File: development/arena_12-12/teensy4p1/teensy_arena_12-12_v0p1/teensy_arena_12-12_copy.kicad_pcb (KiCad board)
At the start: 4 copper layers, 228.6 x 228.6 mm, 51 parts, among them J1 Barrel_Jack, J2 Conn_01x04, J3 Conn_01x04, P1 CONN15, P10 CONN15, P11 CONN15, P12 CONN15, P2 CONN15, P3 CONN15, P4 CONN15, P5 CONN15, P6 CONN15, P7 CONN15, P8 CONN15, P9 CONN15, Q2 MOSFET_NCHAN, SW1 SW_SPDT, U1 TXB0108PW, U18 Teensy4.1, U2 TXB0108PW, U3 TXB0108PW, U4 TXB0108PW, U5 TXB0108PW

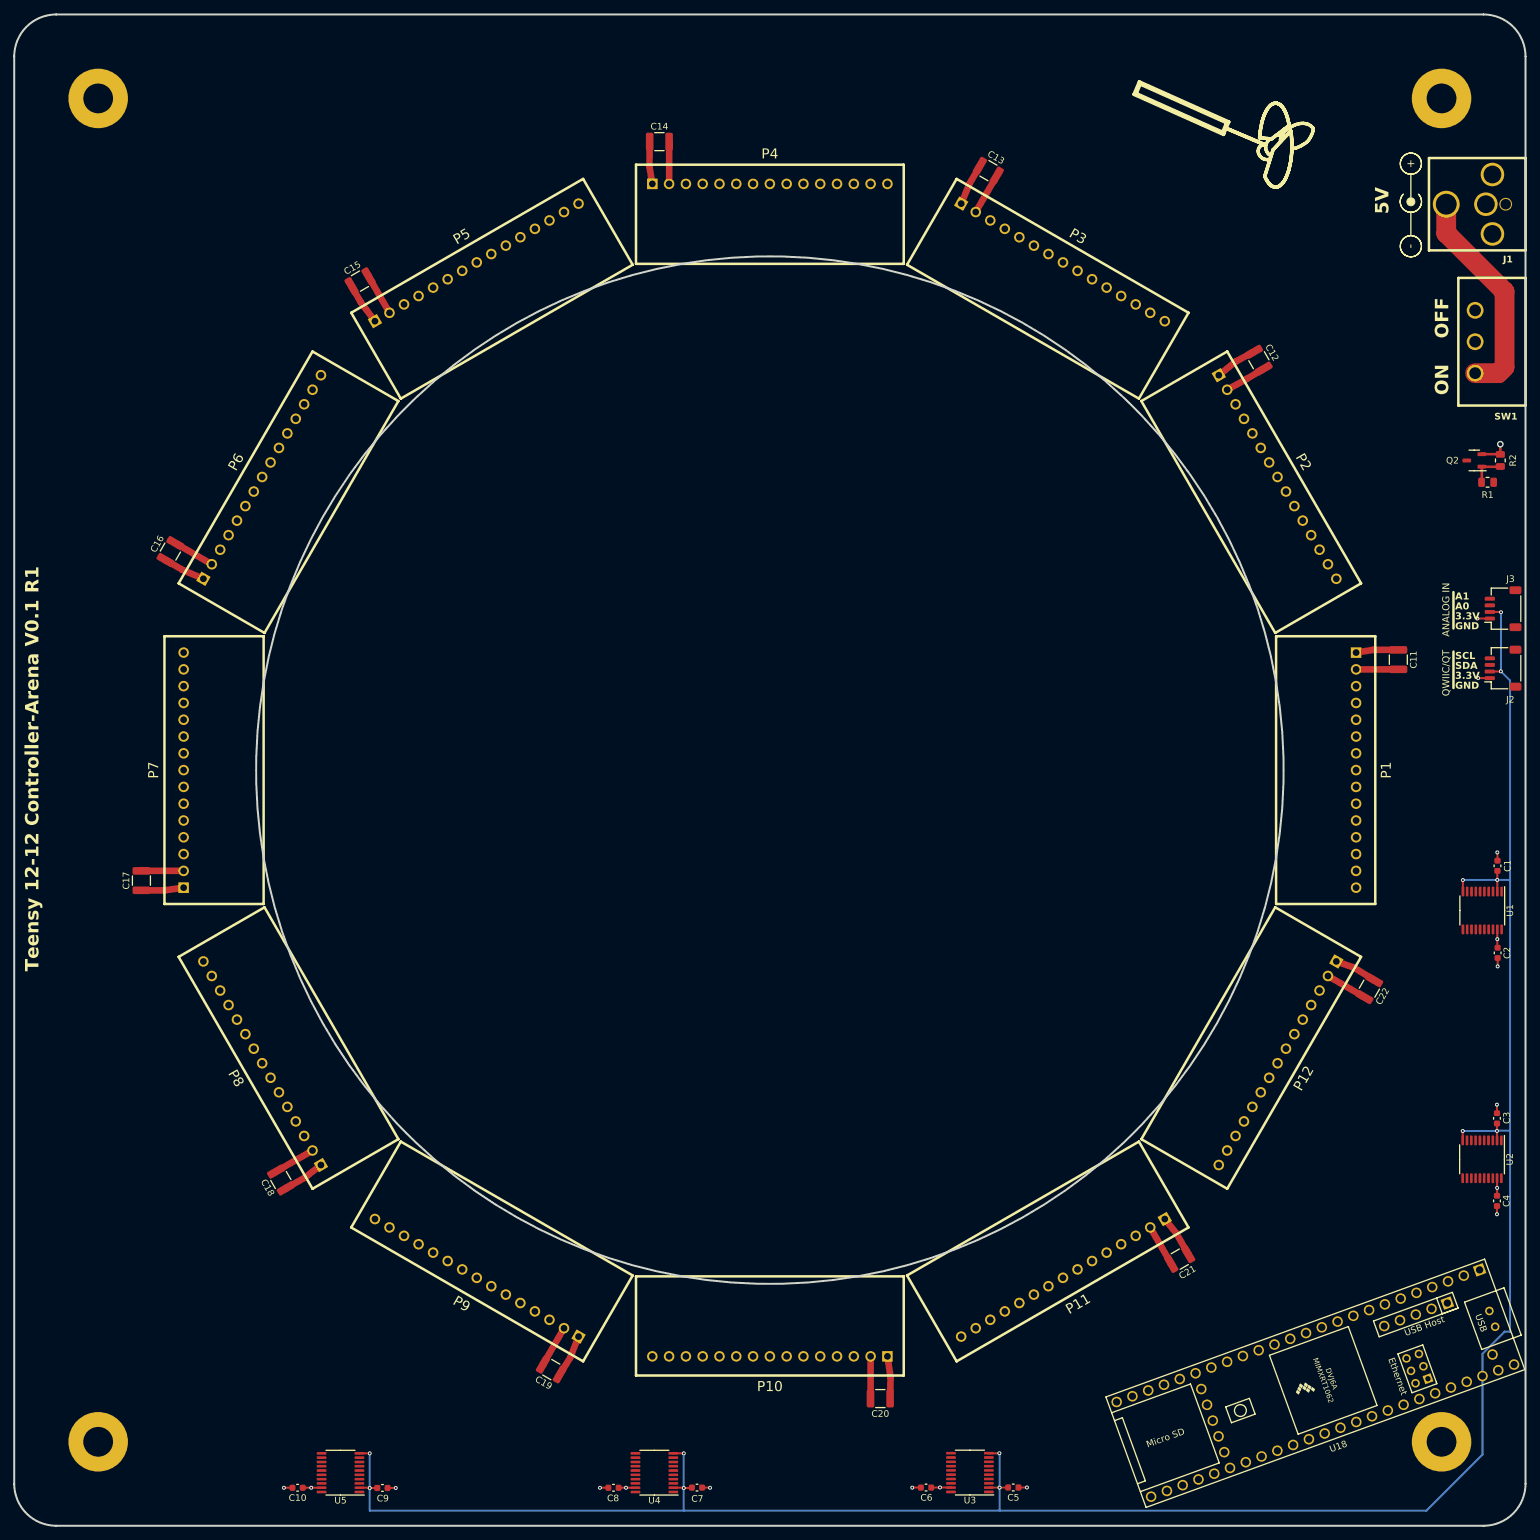
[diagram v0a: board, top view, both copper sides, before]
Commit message: Finished hand route of 12-12 teensy arena. Finished route of 12-12 top.
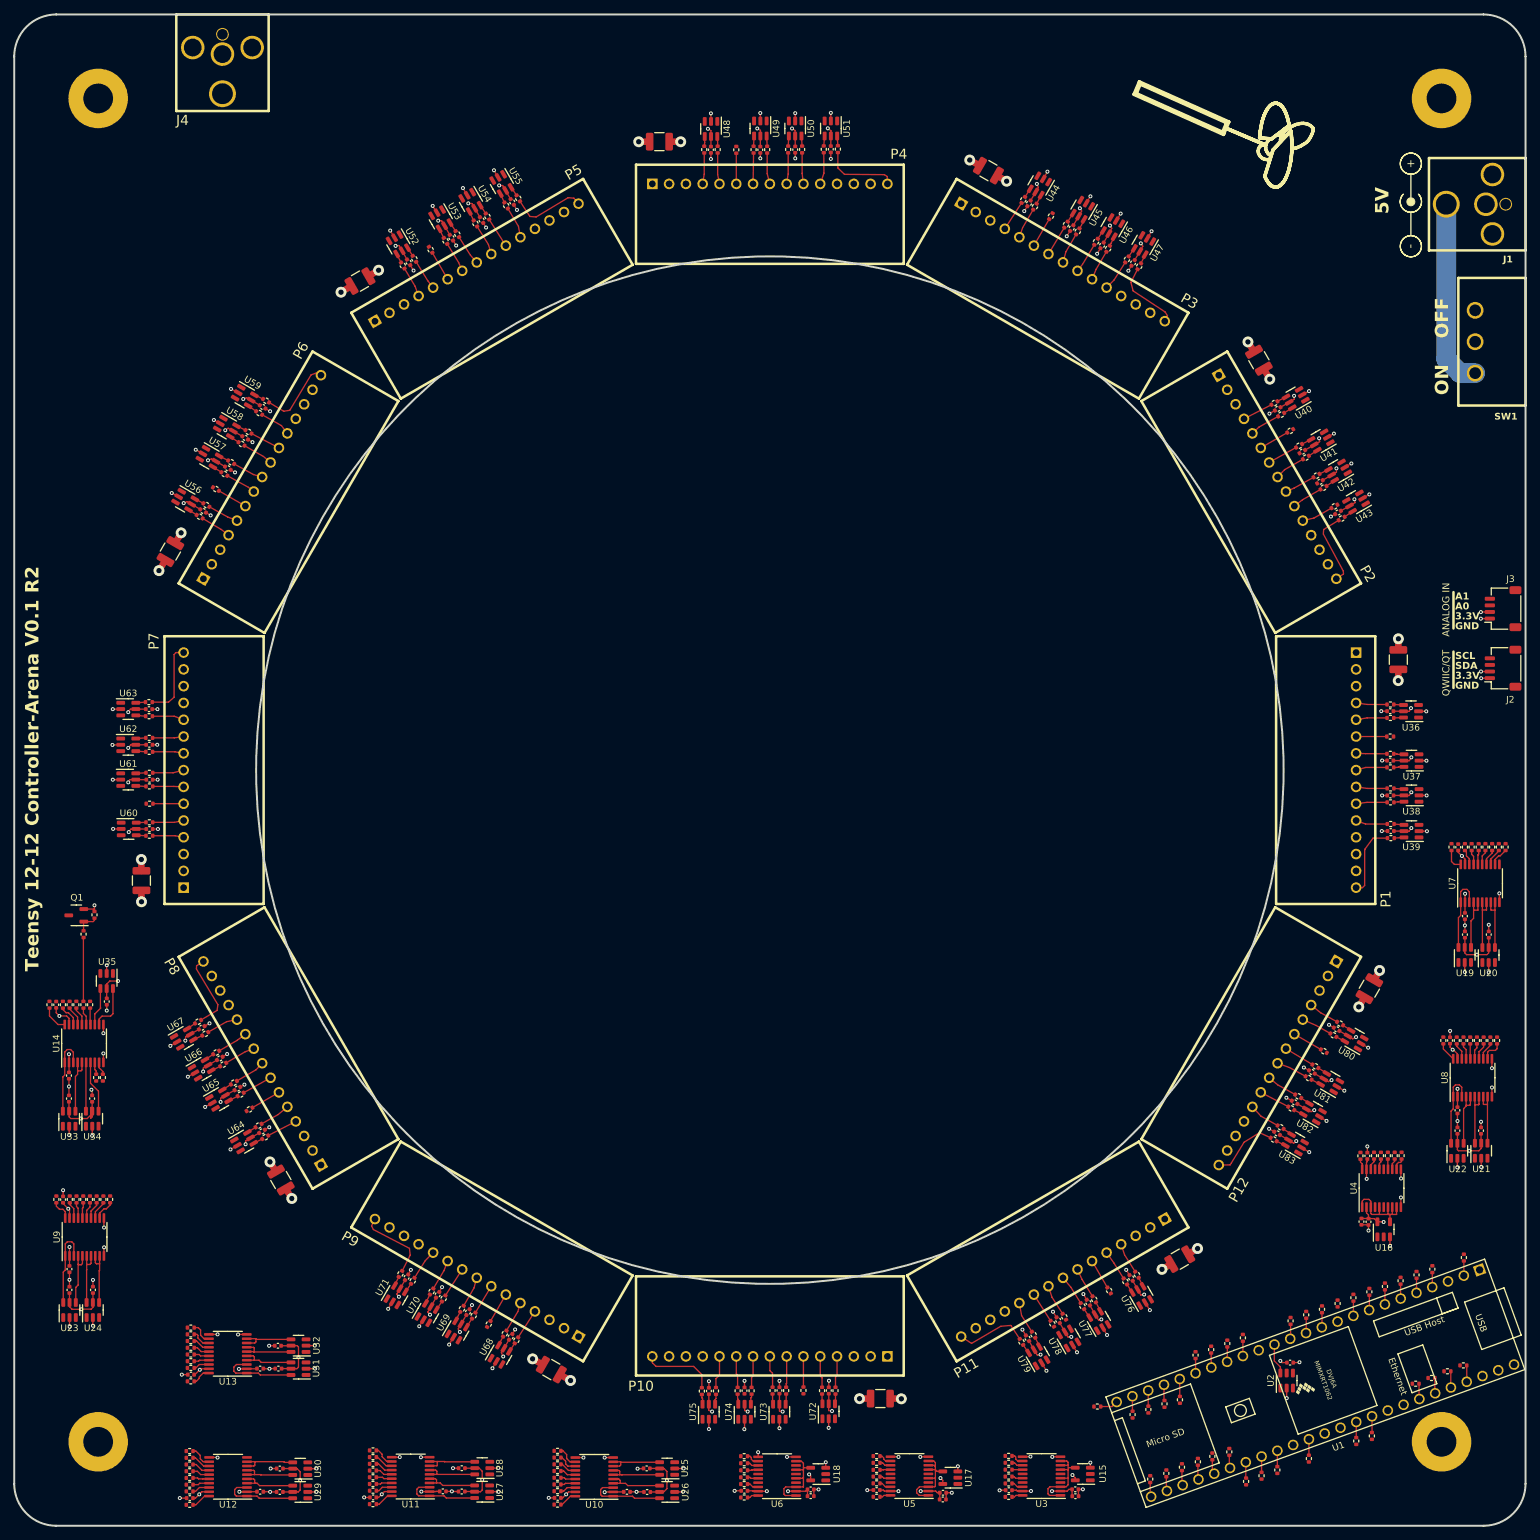
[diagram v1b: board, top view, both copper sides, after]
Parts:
- removed Q2: MOSFET_NCHAN, Package_TO_SOT_SMD:SOT-23-3
- removed the U1 at (285.6, 199.0)
- added C11: 0.1uF, Capacitor_SMD:C_0402_1005Metric, F.Cu at (281.9, 189.5)
- added C12: 0.1uF, Capacitor_SMD:C_0402_1005Metric, F.Cu at (281.8, 229.3)
- added C13: 0.1uF, Capacitor_SMD:C_0402_1005Metric, F.Cu at (280.7, 218.7)
- added C14: 0.1uF, Capacitor_SMD:C_0402_1005Metric, F.Cu at (71.9, 253.3)
- added C15: 0.1uF, Capacitor_SMD:C_0402_1005Metric, F.Cu at (70.9, 242.8)
- added C16: 0.1uF, Capacitor_SMD:C_0402_1005Metric, F.Cu at (156.2, 287.0)
- added C17: 0.1uF, Capacitor_SMD:C_0402_1005Metric, F.Cu at (145.7, 287.9)
- added C18: 0.1uF, Capacitor_SMD:C_0402_1005Metric, F.Cu at (128.3, 286.9)
- added C19: 0.1uF, Capacitor_SMD:C_0402_1005Metric, F.Cu at (117.8, 287.8)
- added C20: 0.1uF, Capacitor_SMD:C_0402_1005Metric, F.Cu at (100.7, 287.0)
- added C21: 0.1uF, Capacitor_SMD:C_0402_1005Metric, F.Cu at (90.1, 287.9)
- added C22: 0.1uF, Capacitor_SMD:C_0402_1005Metric, F.Cu at (100.7, 268.3)
- added C23: 0.1uF, Capacitor_SMD:C_0402_1005Metric, F.Cu at (90.2, 269.2)
- added C24: 0.1uF, Capacitor_SMD:C_0402_1005Metric, F.Cu at (71.8, 224.0)
- added C25: 0.1uF, Capacitor_SMD:C_0402_1005Metric, F.Cu at (69.8, 213.3)
- added C26: 0.1uF, Capacitor_SMD:C_0402_1005Metric, F.Cu at (224.0, 286.6)
- added C27: 0.1uF, Capacitor_SMD:C_0402_1005Metric, F.Cu at (268.4, 246.1)
- added C28: 0.1uF, Capacitor_SMD:C_0402_1005Metric, F.Cu at (204.0, 287.1)
- added C29: 0.1uF, Capacitor_SMD:C_0402_1005Metric, F.Cu at (184.0, 286.6)
- added C30: 0.1uF, Capacitor_SMD:C_0402_1005Metric, F.Cu at (282.9, 202.7)
- added C31: 0.1uF, Capacitor_SMD:C_0402_1005Metric, F.Cu at (286.5, 202.7)
- added C32: 0.1uF, Capacitor_SMD:C_0402_1005Metric, F.Cu at (281.8, 232.3)
- added C33: 0.1uF, Capacitor_SMD:C_0402_1005Metric, F.Cu at (285.4, 232.3)
- added C34: 0.1uF, Capacitor_SMD:C_0402_1005Metric, F.Cu at (71.9, 256.4)
- added C35: 0.1uF, Capacitor_SMD:C_0402_1005Metric, F.Cu at (75.4, 256.4)
- added C36: 0.1uF, Capacitor_SMD:C_0402_1005Metric, F.Cu at (159.2, 283.4)
- added C37: 0.1uF, Capacitor_SMD:C_0402_1005Metric, F.Cu at (159.2, 287.0)
- added C38: 0.1uF, Capacitor_SMD:C_0402_1005Metric, F.Cu at (131.2, 286.9)
- added C39: 0.1uF, Capacitor_SMD:C_0402_1005Metric, F.Cu at (131.2, 283.4)
- added C40: 0.1uF, Capacitor_SMD:C_0402_1005Metric, F.Cu at (103.7, 287.0)
- added C41: 0.1uF, Capacitor_SMD:C_0402_1005Metric, F.Cu at (103.7, 283.4)
- added C42: 0.1uF, Capacitor_SMD:C_0402_1005Metric, F.Cu at (103.5, 268.3)
- added C43: 0.1uF, Capacitor_SMD:C_0402_1005Metric, F.Cu at (103.4, 264.9)
- added C44: 0.1uF, Capacitor_SMD:C_0402_1005Metric, F.Cu at (71.8, 227.5)
- added C45: 0.1uF, Capacitor_SMD:C_0402_1005Metric, F.Cu at (75.3, 227.5)
- added C46: 0.1uF, Capacitor_SMD:C_0402_1005Metric, F.Cu at (77.5, 212.8)
- added C47: 0.1uF, Capacitor_SMD:C_0402_1005Metric, F.Cu at (271.6, 168.9)
- added C48: 0.1uF, Capacitor_SMD:C_0402_1005Metric, F.Cu at (271.6, 176.4)
- added C49: 0.1uF, Capacitor_SMD:C_0402_1005Metric, F.Cu at (271.7, 181.6)
- added C50: 0.1uF, Capacitor_SMD:C_0402_1005Metric, F.Cu at (271.7, 187.0)
- added C51: 0.1uF, Capacitor_SMD:C_0402_1005Metric, F.Cu at (254.6, 123.2)
- added C52: 0.1uF, Capacitor_SMD:C_0402_1005Metric, F.Cu at (258.3, 129.6)
- added C53: 0.1uF, Capacitor_SMD:C_0402_1005Metric, F.Cu at (261.0, 134.2)
- added C54: 0.1uF, Capacitor_SMD:C_0402_1005Metric, F.Cu at (263.7, 138.8)
- added C55: 0.1uF, Capacitor_SMD:C_0402_1005Metric, F.Cu at (217.0, 92.1)
- added C56: 0.1uF, Capacitor_SMD:C_0402_1005Metric, F.Cu at (223.5, 95.8)
- added C57: 0.1uF, Capacitor_SMD:C_0402_1005Metric, F.Cu at (228.1, 98.4)
- added C58: 0.1uF, Capacitor_SMD:C_0402_1005Metric, F.Cu at (232.7, 101.1)
- added C59: 0.1uF, Capacitor_SMD:C_0402_1005Metric, F.Cu at (168.9, 84.0)
- added C60: 0.1uF, Capacitor_SMD:C_0402_1005Metric, F.Cu at (176.4, 84.0)
- added C61: 0.1uF, Capacitor_SMD:C_0402_1005Metric, F.Cu at (181.6, 83.9)
- added C62: 0.1uF, Capacitor_SMD:C_0402_1005Metric, F.Cu at (187.0, 83.9)
- added C63: 0.1uF, Capacitor_SMD:C_0402_1005Metric, F.Cu at (123.2, 101.0)
- added C64: 0.1uF, Capacitor_SMD:C_0402_1005Metric, F.Cu at (129.6, 97.3)
- added C65: 0.1uF, Capacitor_SMD:C_0402_1005Metric, F.Cu at (134.2, 94.6)
- added C66: 0.1uF, Capacitor_SMD:C_0402_1005Metric, F.Cu at (138.8, 91.9)
- added C67: 0.1uF, Capacitor_SMD:C_0402_1005Metric, F.Cu at (92.1, 138.6)
- added C68: 0.1uF, Capacitor_SMD:C_0402_1005Metric, F.Cu at (95.8, 132.1)
- added C69: 0.1uF, Capacitor_SMD:C_0402_1005Metric, F.Cu at (98.4, 127.5)
- added C70: 0.1uF, Capacitor_SMD:C_0402_1005Metric, F.Cu at (101.1, 122.9)
- added C71: 0.1uF, Capacitor_SMD:C_0402_1005Metric, F.Cu at (84.0, 186.7)
- added C72: 0.1uF, Capacitor_SMD:C_0402_1005Metric, F.Cu at (84.0, 179.2)
- added C73: 0.1uF, Capacitor_SMD:C_0402_1005Metric, F.Cu at (83.9, 174.0)
- added C74: 0.1uF, Capacitor_SMD:C_0402_1005Metric, F.Cu at (83.9, 168.6)
- added C75: 0.1uF, Capacitor_SMD:C_0402_1005Metric, F.Cu at (101.0, 232.4)
- added C76: 0.1uF, Capacitor_SMD:C_0402_1005Metric, F.Cu at (97.3, 226.0)
- added C77: 0.1uF, Capacitor_SMD:C_0402_1005Metric, F.Cu at (94.6, 221.4)
- added C78: 0.1uF, Capacitor_SMD:C_0402_1005Metric, F.Cu at (91.9, 216.8)
- added C79: 0.1uF, Capacitor_SMD:C_0402_1005Metric, F.Cu at (138.6, 263.5)
- added C80: 0.1uF, Capacitor_SMD:C_0402_1005Metric, F.Cu at (132.1, 259.8)
- added C81: 0.1uF, Capacitor_SMD:C_0402_1005Metric, F.Cu at (127.5, 257.2)
- added C82: 0.1uF, Capacitor_SMD:C_0402_1005Metric, F.Cu at (122.9, 254.5)
- added C83: 0.1uF, Capacitor_SMD:C_0402_1005Metric, F.Cu at (186.7, 271.6)
- added C84: 0.1uF, Capacitor_SMD:C_0402_1005Metric, F.Cu at (179.2, 271.6)
- added C85: 0.1uF, Capacitor_SMD:C_0402_1005Metric, F.Cu at (174.0, 271.7)
- added C86: 0.1uF, Capacitor_SMD:C_0402_1005Metric, F.Cu at (168.6, 271.7)
- added C87: 0.1uF, Capacitor_SMD:C_0402_1005Metric, F.Cu at (232.4, 254.6)
- added C88: 0.1uF, Capacitor_SMD:C_0402_1005Metric, F.Cu at (226.0, 258.3)
- added C89: 0.1uF, Capacitor_SMD:C_0402_1005Metric, F.Cu at (221.4, 261.0)
- added C90: 0.1uF, Capacitor_SMD:C_0402_1005Metric, F.Cu at (216.8, 263.7)
- added C91: 0.1uF, Capacitor_SMD:C_0402_1005Metric, F.Cu at (263.5, 217.0)
- added C92: 0.1uF, Capacitor_SMD:C_0402_1005Metric, F.Cu at (259.8, 223.5)
- added C93: 0.1uF, Capacitor_SMD:C_0402_1005Metric, F.Cu at (257.2, 228.1)
- added C94: 0.1uF, Capacitor_SMD:C_0402_1005Metric, F.Cu at (254.5, 232.7)
- added J4: Barrel_Jack, arena_custom:DCJACK_2PIN_HIGHCURRENT, F.Cu at (95.0, 63.5)
- added Q1: MOSFET_NCHAN, Package_TO_SOT_SMD:SOT-23-3, F.Cu at (72.9, 199.8)
- added R10: 68, Resistor_SMD:R_0402_1005Metric, F.Cu at (275.6, 254.2)
- added R100: 68, Resistor_SMD:R_0402_1005Metric, F.Cu at (117.8, 282.7)
- added R101: 68, Resistor_SMD:R_0402_1005Metric, F.Cu at (117.8, 281.7)
- added R102: 68, Resistor_SMD:R_0402_1005Metric, F.Cu at (117.8, 280.7)
- added R103: 68, Resistor_SMD:R_0402_1005Metric, F.Cu at (90.0, 288.9)
- added R104: 68, Resistor_SMD:R_0402_1005Metric, F.Cu at (90.0, 286.9)
- added R105: 68, Resistor_SMD:R_0402_1005Metric, F.Cu at (90.0, 285.9)
- added R106: 68, Resistor_SMD:R_0402_1005Metric, F.Cu at (90.0, 284.9)
- added R107: 68, Resistor_SMD:R_0402_1005Metric, F.Cu at (90.0, 283.9)
- added R108: 68, Resistor_SMD:R_0402_1005Metric, F.Cu at (90.0, 282.8)
- added R109: 68, Resistor_SMD:R_0402_1005Metric, F.Cu at (90.0, 281.8)
- added R11: 68, Resistor_SMD:R_0402_1005Metric, F.Cu at (273.2, 255.0)
- added R110: 68, Resistor_SMD:R_0402_1005Metric, F.Cu at (90.0, 280.8)
- added R111: 68, Resistor_SMD:R_0402_1005Metric, F.Cu at (90.2, 270.3)
- added R112: 68, Resistor_SMD:R_0402_1005Metric, F.Cu at (90.2, 268.2)
- added R113: 68, Resistor_SMD:R_0402_1005Metric, F.Cu at (90.2, 267.2)
- added R114: 68, Resistor_SMD:R_0402_1005Metric, F.Cu at (90.2, 266.2)
- added R115: 68, Resistor_SMD:R_0402_1005Metric, F.Cu at (90.2, 265.2)
- added R116: 68, Resistor_SMD:R_0402_1005Metric, F.Cu at (90.2, 264.2)
- added R117: 68, Resistor_SMD:R_0402_1005Metric, F.Cu at (90.2, 263.1)
- added R118: 68, Resistor_SMD:R_0402_1005Metric, F.Cu at (90.2, 262.1)
- added R119: 68, Resistor_SMD:R_0402_1005Metric, F.Cu at (68.8, 213.3)
- added R12: 68, Resistor_SMD:R_0402_1005Metric, F.Cu at (270.8, 255.9)
- added R120: 68, Resistor_SMD:R_0402_1005Metric, F.Cu at (70.9, 213.3)
- added R121: 68, Resistor_SMD:R_0402_1005Metric, F.Cu at (71.9, 213.3)
- added R122: 68, Resistor_SMD:R_0402_1005Metric, F.Cu at (72.9, 213.3)
- added R123: 68, Resistor_SMD:R_0402_1005Metric, F.Cu at (74.0, 213.3)
- added R124: 68, Resistor_SMD:R_0402_1005Metric, F.Cu at (75.0, 213.3)
- added R125: 68, Resistor_SMD:R_0402_1005Metric, F.Cu at (75.9, 224.3)
- added R126: 68, Resistor_SMD:R_0402_1005Metric, F.Cu at (76.9, 224.3)
- added R127: 68, Resistor_SMD:R_0402_1005Metric, F.Cu at (271.7, 167.9)
- added R128: 68, Resistor_SMD:R_0402_1005Metric, F.Cu at (271.7, 169.9)
- added R129: 68, Resistor_SMD:R_0402_1005Metric, F.Cu at (271.7, 175.3)
- added R13: 68, Resistor_SMD:R_0402_1005Metric, F.Cu at (268.5, 256.7)
- added R130: 68, Resistor_SMD:R_0402_1005Metric, F.Cu at (271.7, 177.4)
- added R131: 68, Resistor_SMD:R_0402_1005Metric, F.Cu at (271.7, 180.6)
- added R132: 68, Resistor_SMD:R_0402_1005Metric, F.Cu at (271.7, 182.7)
- added R133: 68, Resistor_SMD:R_0402_1005Metric, F.Cu at (271.7, 186.0)
- added R134: 68, Resistor_SMD:R_0402_1005Metric, F.Cu at (271.7, 188.1)
- added R135: 68, Resistor_SMD:R_0402_1005Metric, F.Cu at (254.1, 122.3)
- added R136: 68, Resistor_SMD:R_0402_1005Metric, F.Cu at (255.1, 124.0)
- added R137: 68, Resistor_SMD:R_0402_1005Metric, F.Cu at (257.8, 128.7)
- added R138: 68, Resistor_SMD:R_0402_1005Metric, F.Cu at (258.9, 130.5)
- added R139: 68, Resistor_SMD:R_0402_1005Metric, F.Cu at (260.5, 133.3)
- added R14: 68, Resistor_SMD:R_0402_1005Metric, F.Cu at (266.1, 257.6)
- added R140: 68, Resistor_SMD:R_0402_1005Metric, F.Cu at (261.5, 135.1)
- added R141: 68, Resistor_SMD:R_0402_1005Metric, F.Cu at (263.2, 137.9)
- added R142: 68, Resistor_SMD:R_0402_1005Metric, F.Cu at (264.3, 139.7)
- added R143: 68, Resistor_SMD:R_0402_1005Metric, F.Cu at (216.1, 91.5)
- added R144: 68, Resistor_SMD:R_0402_1005Metric, F.Cu at (217.9, 92.6)
- added R145: 68, Resistor_SMD:R_0402_1005Metric, F.Cu at (222.6, 95.3)
- added R146: 68, Resistor_SMD:R_0402_1005Metric, F.Cu at (224.4, 96.3)
- added R147: 68, Resistor_SMD:R_0402_1005Metric, F.Cu at (227.1, 97.9)
- added R148: 68, Resistor_SMD:R_0402_1005Metric, F.Cu at (229.0, 98.9)
- added R149: 68, Resistor_SMD:R_0402_1005Metric, F.Cu at (231.8, 100.6)
- added R15: 68, Resistor_SMD:R_0402_1005Metric, F.Cu at (263.7, 258.5)
- added R150: 68, Resistor_SMD:R_0402_1005Metric, F.Cu at (233.7, 101.6)
- added R151: 68, Resistor_SMD:R_0402_1005Metric, F.Cu at (167.9, 83.9)
- added R152: 68, Resistor_SMD:R_0402_1005Metric, F.Cu at (169.9, 83.9)
- added R153: 68, Resistor_SMD:R_0402_1005Metric, F.Cu at (175.3, 83.9)
- added R154: 68, Resistor_SMD:R_0402_1005Metric, F.Cu at (177.4, 83.9)
- added R155: 68, Resistor_SMD:R_0402_1005Metric, F.Cu at (180.6, 83.9)
- added R156: 68, Resistor_SMD:R_0402_1005Metric, F.Cu at (182.7, 83.9)
- added R157: 68, Resistor_SMD:R_0402_1005Metric, F.Cu at (186.0, 83.9)
- added R158: 68, Resistor_SMD:R_0402_1005Metric, F.Cu at (188.1, 83.9)
- added R159: 68, Resistor_SMD:R_0402_1005Metric, F.Cu at (122.3, 101.5)
- added R16: 68, Resistor_SMD:R_0402_1005Metric, F.Cu at (261.3, 259.4)
- added R160: 68, Resistor_SMD:R_0402_1005Metric, F.Cu at (124.0, 100.5)
- added R161: 68, Resistor_SMD:R_0402_1005Metric, F.Cu at (128.7, 97.8)
- added R162: 68, Resistor_SMD:R_0402_1005Metric, F.Cu at (130.5, 96.7)
- added R163: 68, Resistor_SMD:R_0402_1005Metric, F.Cu at (133.3, 95.1)
- added R164: 68, Resistor_SMD:R_0402_1005Metric, F.Cu at (135.1, 94.1)
- added R165: 68, Resistor_SMD:R_0402_1005Metric, F.Cu at (137.9, 92.4)
- added R166: 68, Resistor_SMD:R_0402_1005Metric, F.Cu at (139.7, 91.3)
- added R167: 68, Resistor_SMD:R_0402_1005Metric, F.Cu at (91.5, 139.5)
- added R168: 68, Resistor_SMD:R_0402_1005Metric, F.Cu at (92.6, 137.7)
- added R169: 68, Resistor_SMD:R_0402_1005Metric, F.Cu at (95.3, 133.0)
- added R17: 68, Resistor_SMD:R_0402_1005Metric, F.Cu at (258.9, 260.2)
- added R170: 68, Resistor_SMD:R_0402_1005Metric, F.Cu at (96.3, 131.2)
- added R171: 68, Resistor_SMD:R_0402_1005Metric, F.Cu at (97.9, 128.5)
- added R172: 68, Resistor_SMD:R_0402_1005Metric, F.Cu at (98.9, 126.6)
- added R173: 68, Resistor_SMD:R_0402_1005Metric, F.Cu at (100.6, 123.8)
- added R174: 68, Resistor_SMD:R_0402_1005Metric, F.Cu at (101.6, 121.9)
- added R175: 68, Resistor_SMD:R_0402_1005Metric, F.Cu at (83.9, 187.7)
- added R176: 68, Resistor_SMD:R_0402_1005Metric, F.Cu at (83.9, 185.7)
- added R177: 68, Resistor_SMD:R_0402_1005Metric, F.Cu at (83.9, 180.3)
- added R178: 68, Resistor_SMD:R_0402_1005Metric, F.Cu at (83.9, 178.2)
- added R179: 68, Resistor_SMD:R_0402_1005Metric, F.Cu at (83.9, 175.0)
- added R18: 68, Resistor_SMD:R_0402_1005Metric, F.Cu at (249.4, 263.7)
- added R180: 68, Resistor_SMD:R_0402_1005Metric, F.Cu at (83.9, 172.9)
- added R181: 68, Resistor_SMD:R_0402_1005Metric, F.Cu at (83.9, 169.6)
- added R182: 68, Resistor_SMD:R_0402_1005Metric, F.Cu at (83.9, 167.5)
- added R183: 68, Resistor_SMD:R_0402_1005Metric, F.Cu at (101.5, 233.3)
- added R184: 68, Resistor_SMD:R_0402_1005Metric, F.Cu at (100.5, 231.6)
- added R185: 68, Resistor_SMD:R_0402_1005Metric, F.Cu at (97.8, 226.9)
- added R186: 68, Resistor_SMD:R_0402_1005Metric, F.Cu at (96.7, 225.1)
- added R187: 68, Resistor_SMD:R_0402_1005Metric, F.Cu at (95.1, 222.3)
- added R188: 68, Resistor_SMD:R_0402_1005Metric, F.Cu at (94.1, 220.5)
- added R189: 68, Resistor_SMD:R_0402_1005Metric, F.Cu at (92.4, 217.7)
- added R19: 68, Resistor_SMD:R_0402_1005Metric, F.Cu at (247.0, 264.5)
- added R190: 68, Resistor_SMD:R_0402_1005Metric, F.Cu at (91.3, 215.9)
- added R191: 68, Resistor_SMD:R_0402_1005Metric, F.Cu at (139.5, 264.1)
- added R192: 68, Resistor_SMD:R_0402_1005Metric, F.Cu at (137.7, 263.0)
- added R193: 68, Resistor_SMD:R_0402_1005Metric, F.Cu at (133.0, 260.3)
- added R194: 68, Resistor_SMD:R_0402_1005Metric, F.Cu at (131.2, 259.3)
- added R195: 68, Resistor_SMD:R_0402_1005Metric, F.Cu at (128.5, 257.7)
- added R196: 68, Resistor_SMD:R_0402_1005Metric, F.Cu at (126.6, 256.7)
- added R197: 68, Resistor_SMD:R_0402_1005Metric, F.Cu at (123.8, 255.0)
- added R198: 68, Resistor_SMD:R_0402_1005Metric, F.Cu at (121.9, 254.0)
- added R199: 68, Resistor_SMD:R_0402_1005Metric, F.Cu at (187.7, 271.7)
- added R20: 68, Resistor_SMD:R_0402_1005Metric, F.Cu at (239.8, 273.1)
- added R200: 68, Resistor_SMD:R_0402_1005Metric, F.Cu at (185.7, 271.7)
- added R201: 68, Resistor_SMD:R_0402_1005Metric, F.Cu at (180.3, 271.7)
- added R202: 68, Resistor_SMD:R_0402_1005Metric, F.Cu at (178.2, 271.7)
- added R203: 68, Resistor_SMD:R_0402_1005Metric, F.Cu at (175.0, 271.7)
- added R204: 68, Resistor_SMD:R_0402_1005Metric, F.Cu at (172.9, 271.7)
- added R205: 68, Resistor_SMD:R_0402_1005Metric, F.Cu at (169.6, 271.7)
- added R206: 68, Resistor_SMD:R_0402_1005Metric, F.Cu at (167.5, 271.7)
- added R207: 68, Resistor_SMD:R_0402_1005Metric, F.Cu at (233.3, 254.1)
- added R208: 68, Resistor_SMD:R_0402_1005Metric, F.Cu at (231.6, 255.1)
- added R209: 68, Resistor_SMD:R_0402_1005Metric, F.Cu at (226.9, 257.8)
- added R21: 68, Resistor_SMD:R_0402_1005Metric, F.Cu at (237.5, 273.7)
- added R210: 68, Resistor_SMD:R_0402_1005Metric, F.Cu at (225.1, 258.9)
- added R211: 68, Resistor_SMD:R_0402_1005Metric, F.Cu at (222.3, 260.5)
- added R212: 68, Resistor_SMD:R_0402_1005Metric, F.Cu at (220.5, 261.5)
- added R213: 68, Resistor_SMD:R_0402_1005Metric, F.Cu at (217.7, 263.2)
- added R214: 68, Resistor_SMD:R_0402_1005Metric, F.Cu at (215.9, 264.3)
- added R215: 68, Resistor_SMD:R_0402_1005Metric, F.Cu at (264.1, 216.1)
- added R216: 68, Resistor_SMD:R_0402_1005Metric, F.Cu at (263.0, 217.9)
- added R217: 68, Resistor_SMD:R_0402_1005Metric, F.Cu at (260.3, 222.6)
- added R218: 68, Resistor_SMD:R_0402_1005Metric, F.Cu at (259.3, 224.4)
- added R219: 68, Resistor_SMD:R_0402_1005Metric, F.Cu at (257.7, 227.1)
- added R22: 68, Resistor_SMD:R_0402_1005Metric, F.Cu at (235.1, 274.5)
- added R220: 68, Resistor_SMD:R_0402_1005Metric, F.Cu at (256.7, 229.0)
- added R221: 68, Resistor_SMD:R_0402_1005Metric, F.Cu at (255.0, 231.8)
- added R222: 68, Resistor_SMD:R_0402_1005Metric, F.Cu at (254.0, 233.7)
- added R223: 68, Resistor_SMD:R_0402_1005Metric, F.Cu at (271.6, 172.7)
- added R224: 68, Resistor_SMD:R_0402_1005Metric, F.Cu at (256.5, 126.5)
- added R225: 68, Resistor_SMD:R_0402_1005Metric, F.Cu at (220.3, 94.0)
- added R226: 68, Resistor_SMD:R_0402_1005Metric, F.Cu at (172.7, 84.0)
- added R227: 68, Resistor_SMD:R_0402_1005Metric, F.Cu at (126.5, 99.1)
- added R228: 68, Resistor_SMD:R_0402_1005Metric, F.Cu at (94.0, 135.3)
- added R229: 68, Resistor_SMD:R_0402_1005Metric, F.Cu at (84.0, 182.9)
- added R23: 68, Resistor_SMD:R_0402_1005Metric, F.Cu at (232.7, 275.3)
- added R230: 68, Resistor_SMD:R_0402_1005Metric, F.Cu at (99.1, 229.1)
- added R231: 68, Resistor_SMD:R_0402_1005Metric, F.Cu at (135.3, 261.6)
- added R232: 68, Resistor_SMD:R_0402_1005Metric, F.Cu at (182.9, 271.6)
- added R233: 68, Resistor_SMD:R_0402_1005Metric, F.Cu at (229.1, 256.5)
- added R234: 68, Resistor_SMD:R_0402_1005Metric, F.Cu at (261.6, 220.3)
- added R24: 68, Resistor_SMD:R_0402_1005Metric, F.Cu at (227.3, 274.1)
- added R25: 68, Resistor_SMD:R_0402_1005Metric, F.Cu at (282.7, 267.8)
- added R26: 68, Resistor_SMD:R_0402_1005Metric, F.Cu at (280.3, 268.7)
- added R27: 68, Resistor_SMD:R_0402_1005Metric, F.Cu at (277.9, 269.7)
- added R28: 68, Resistor_SMD:R_0402_1005Metric, F.Cu at (275.5, 270.6)
- added R29: 68, Resistor_SMD:R_0402_1005Metric, F.Cu at (268.9, 278.5)
- added R3: 68, Resistor_SMD:R_0402_1005Metric, F.Cu at (237.8, 284.2)
- added R30: 68, Resistor_SMD:R_0402_1005Metric, F.Cu at (266.5, 279.3)
- added R31: 68, Resistor_SMD:R_0402_1005Metric, F.Cu at (254.6, 283.7)
- added R32: 68, Resistor_SMD:R_0402_1005Metric, F.Cu at (252.2, 284.5)
- added R33: 68, Resistor_SMD:R_0402_1005Metric, F.Cu at (249.8, 285.4)
- added R34: 68, Resistor_SMD:R_0402_1005Metric, F.Cu at (247.3, 280.9)
- added R35: 68, Resistor_SMD:R_0402_1005Metric, F.Cu at (244.7, 281.6)
- added R36: 68, Resistor_SMD:R_0402_1005Metric, F.Cu at (242.5, 282.4)
- added R37: 68, Resistor_SMD:R_0402_1005Metric, F.Cu at (240.1, 283.2)
- added R38: 68, Resistor_SMD:R_0402_1005Metric, F.Cu at (235.3, 285.0)
- added R39: 68, Resistor_SMD:R_0402_1005Metric, F.Cu at (213.9, 287.7)
- added R4: 68, Resistor_SMD:R_0402_1005Metric, F.Cu at (259.3, 281.9)
- added R40: 68, Resistor_SMD:R_0402_1005Metric, F.Cu at (213.9, 285.7)
- added R41: 68, Resistor_SMD:R_0402_1005Metric, F.Cu at (213.9, 284.7)
- added R42: 68, Resistor_SMD:R_0402_1005Metric, F.Cu at (213.9, 283.6)
- added R43: 68, Resistor_SMD:R_0402_1005Metric, F.Cu at (213.9, 282.6)
- added R44: 68, Resistor_SMD:R_0402_1005Metric, F.Cu at (213.9, 281.5)
- added R45: 68, Resistor_SMD:R_0402_1005Metric, F.Cu at (267.1, 236.1)
- added R46: 68, Resistor_SMD:R_0402_1005Metric, F.Cu at (269.2, 236.1)
- added R47: 68, Resistor_SMD:R_0402_1005Metric, F.Cu at (270.2, 236.1)
- added R48: 68, Resistor_SMD:R_0402_1005Metric, F.Cu at (271.3, 236.1)
- added R49: 68, Resistor_SMD:R_0402_1005Metric, F.Cu at (272.3, 236.1)
- added R5: 68, Resistor_SMD:R_0402_1005Metric, F.Cu at (256.6, 261.1)
- added R50: 68, Resistor_SMD:R_0402_1005Metric, F.Cu at (273.4, 236.1)
- added R51: 68, Resistor_SMD:R_0402_1005Metric, F.Cu at (193.9, 287.7)
- added R52: 68, Resistor_SMD:R_0402_1005Metric, F.Cu at (193.9, 285.7)
- added R53: 68, Resistor_SMD:R_0402_1005Metric, F.Cu at (193.9, 284.7)
- added R54: 68, Resistor_SMD:R_0402_1005Metric, F.Cu at (193.9, 283.7)
- added R55: 68, Resistor_SMD:R_0402_1005Metric, F.Cu at (193.9, 282.6)
- added R56: 68, Resistor_SMD:R_0402_1005Metric, F.Cu at (193.9, 281.6)
- added R57: 68, Resistor_SMD:R_0402_1005Metric, F.Cu at (173.9, 287.8)
- added R58: 68, Resistor_SMD:R_0402_1005Metric, F.Cu at (173.9, 285.8)
- added R59: 68, Resistor_SMD:R_0402_1005Metric, F.Cu at (173.9, 284.8)
- added R6: 68, Resistor_SMD:R_0402_1005Metric, F.Cu at (242.2, 266.3)
- added R60: 68, Resistor_SMD:R_0402_1005Metric, F.Cu at (173.9, 283.7)
- added R61: 68, Resistor_SMD:R_0402_1005Metric, F.Cu at (173.9, 282.6)
- added R62: 68, Resistor_SMD:R_0402_1005Metric, F.Cu at (173.9, 281.6)
- added R63: 68, Resistor_SMD:R_0402_1005Metric, F.Cu at (282.9, 189.4)
- added R64: 68, Resistor_SMD:R_0402_1005Metric, F.Cu at (284.0, 189.4)
- added R65: 68, Resistor_SMD:R_0402_1005Metric, F.Cu at (285.0, 189.4)
- added R66: 68, Resistor_SMD:R_0402_1005Metric, F.Cu at (286.0, 189.4)
- added R67: 68, Resistor_SMD:R_0402_1005Metric, F.Cu at (287.1, 189.4)
- added R68: 68, Resistor_SMD:R_0402_1005Metric, F.Cu at (288.1, 189.4)
- added R69: 68, Resistor_SMD:R_0402_1005Metric, F.Cu at (280.9, 189.4)
- added R7: 68, Resistor_SMD:R_0402_1005Metric, F.Cu at (244.6, 265.5)
- added R70: 68, Resistor_SMD:R_0402_1005Metric, F.Cu at (289.1, 189.4)
- added R71: 68, Resistor_SMD:R_0402_1005Metric, F.Cu at (279.7, 218.7)
- added R72: 68, Resistor_SMD:R_0402_1005Metric, F.Cu at (281.7, 218.7)
- added R73: 68, Resistor_SMD:R_0402_1005Metric, F.Cu at (282.7, 218.7)
- added R74: 68, Resistor_SMD:R_0402_1005Metric, F.Cu at (283.7, 218.7)
- added R75: 68, Resistor_SMD:R_0402_1005Metric, F.Cu at (284.7, 218.7)
- added R76: 68, Resistor_SMD:R_0402_1005Metric, F.Cu at (285.8, 218.7)
- added R77: 68, Resistor_SMD:R_0402_1005Metric, F.Cu at (286.8, 218.7)
- added R78: 68, Resistor_SMD:R_0402_1005Metric, F.Cu at (287.8, 218.7)
- added R79: 68, Resistor_SMD:R_0402_1005Metric, F.Cu at (69.9, 242.7)
- added R8: 68, Resistor_SMD:R_0402_1005Metric, F.Cu at (282.8, 251.5)
- added R80: 68, Resistor_SMD:R_0402_1005Metric, F.Cu at (71.9, 242.7)
- added R81: 68, Resistor_SMD:R_0402_1005Metric, F.Cu at (72.9, 242.7)
- added R82: 68, Resistor_SMD:R_0402_1005Metric, F.Cu at (73.9, 242.7)
- added R83: 68, Resistor_SMD:R_0402_1005Metric, F.Cu at (75.0, 242.7)
- added R84: 68, Resistor_SMD:R_0402_1005Metric, F.Cu at (76.0, 242.7)
- added R85: 68, Resistor_SMD:R_0402_1005Metric, F.Cu at (77.0, 242.7)
- added R86: 68, Resistor_SMD:R_0402_1005Metric, F.Cu at (78.0, 242.7)
- added R87: 68, Resistor_SMD:R_0402_1005Metric, F.Cu at (145.7, 288.9)
- added R88: 68, Resistor_SMD:R_0402_1005Metric, F.Cu at (145.7, 286.9)
- added R89: 68, Resistor_SMD:R_0402_1005Metric, F.Cu at (145.7, 285.9)
- added R9: 68, Resistor_SMD:R_0402_1005Metric, F.Cu at (278.0, 253.3)
- added R90: 68, Resistor_SMD:R_0402_1005Metric, F.Cu at (145.7, 284.8)
- added R91: 68, Resistor_SMD:R_0402_1005Metric, F.Cu at (145.7, 283.8)
- added R92: 68, Resistor_SMD:R_0402_1005Metric, F.Cu at (145.7, 282.8)
- added R93: 68, Resistor_SMD:R_0402_1005Metric, F.Cu at (145.7, 281.8)
- added R94: 68, Resistor_SMD:R_0402_1005Metric, F.Cu at (145.7, 280.8)
- added R95: 68, Resistor_SMD:R_0402_1005Metric, F.Cu at (117.8, 288.8)
- added R96: 68, Resistor_SMD:R_0402_1005Metric, F.Cu at (117.8, 286.8)
- added R97: 68, Resistor_SMD:R_0402_1005Metric, F.Cu at (117.8, 285.8)
- added R98: 68, Resistor_SMD:R_0402_1005Metric, F.Cu at (117.8, 284.8)
- added R99: 68, Resistor_SMD:R_0402_1005Metric, F.Cu at (117.8, 283.7)
- added U10: TXB0108PW, Package_SO:TSSOP-20_4.4x6.5mm_P0.65mm, F.Cu at (151.2, 284.7)
- added U11: TXB0108PW, Package_SO:TSSOP-20_4.4x6.5mm_P0.65mm, F.Cu at (123.5, 284.7)
- added U12: TXB0108PW, Package_SO:TSSOP-20_4.4x6.5mm_P0.65mm, F.Cu at (95.8, 284.7)
- added U13: TXB0108PW, Package_SO:TSSOP-20_4.4x6.5mm_P0.65mm, F.Cu at (95.8, 266.1)
- added U14: TXB0108PW, Package_SO:TSSOP-20_4.4x6.5mm_P0.65mm, F.Cu at (74.1, 219.1)
- added U15: 74LVC1G17, Package_TO_SOT_SMD:SOT-23-5, F.Cu at (225.1, 284.3)
- added U16: 74LVC1G17, Package_TO_SOT_SMD:SOT-23-5, F.Cu at (270.6, 247.3)
- added U17: 74LVC1G17, Package_TO_SOT_SMD:SOT-23-5, F.Cu at (205.1, 284.8)
- added U18: 74LVC1G17, Package_TO_SOT_SMD:SOT-23-5, F.Cu at (185.1, 284.3)
- added U19: 74LVC2G17, Package_TO_SOT_SMD:SOT-23-6, F.Cu at (282.9, 205.8)
- added U20: 74LVC2G17, Package_TO_SOT_SMD:SOT-23-6, F.Cu at (286.5, 205.8)
- added U21: 74LVC2G17, Package_TO_SOT_SMD:SOT-23-6, F.Cu at (285.4, 235.4)
- added U22: 74LVC2G17, Package_TO_SOT_SMD:SOT-23-6, F.Cu at (281.8, 235.4)
- added U23: 74LVC2G17, Package_TO_SOT_SMD:SOT-23-6, F.Cu at (71.9, 259.5)
- added U24: 74LVC2G17, Package_TO_SOT_SMD:SOT-23-6, F.Cu at (75.4, 259.5)
- added U25: 74LVC2G17, Package_TO_SOT_SMD:SOT-23-6, F.Cu at (162.3, 283.4)
- added U26: 74LVC2G17, Package_TO_SOT_SMD:SOT-23-6, F.Cu at (162.3, 287.0)
- added U27: 74LVC2G17, Package_TO_SOT_SMD:SOT-23-6, F.Cu at (134.3, 287.0)
- added U28: 74LVC2G17, Package_TO_SOT_SMD:SOT-23-6, F.Cu at (134.3, 283.4)
- added U29: 74LVC2G17, Package_TO_SOT_SMD:SOT-23-6, F.Cu at (106.8, 287.0)
- added U30: 74LVC2G17, Package_TO_SOT_SMD:SOT-23-6, F.Cu at (106.8, 283.5)
- added U31: 74LVC2G17, Package_TO_SOT_SMD:SOT-23-6, F.Cu at (106.5, 268.3)
- added U32: 74LVC2G17, Package_TO_SOT_SMD:SOT-23-6, F.Cu at (106.5, 264.9)
- added U33: 74LVC2G17, Package_TO_SOT_SMD:SOT-23-6, F.Cu at (71.8, 230.5)
- added U34: 74LVC2G17, Package_TO_SOT_SMD:SOT-23-6, F.Cu at (75.3, 230.5)
- added U35: 74LVC2G17, Package_TO_SOT_SMD:SOT-23-6, F.Cu at (77.5, 209.7)
- added U36: 74LVC2G17, Package_TO_SOT_SMD:SOT-23-6, F.Cu at (274.8, 168.9)
- added U37: 74LVC2G17, Package_TO_SOT_SMD:SOT-23-6, F.Cu at (274.9, 176.4)
- added U38: 74LVC2G17, Package_TO_SOT_SMD:SOT-23-6, F.Cu at (274.9, 181.6)
- added U39: 74LVC2G17, Package_TO_SOT_SMD:SOT-23-6, F.Cu at (274.9, 187.0)
- added U40: 74LVC2G17, Package_TO_SOT_SMD:SOT-23-6, F.Cu at (257.3, 121.6)
- added U41: 74LVC2G17, Package_TO_SOT_SMD:SOT-23-6, F.Cu at (261.1, 128.0)
- added U42: 74LVC2G17, Package_TO_SOT_SMD:SOT-23-6, F.Cu at (263.8, 132.6)
- added U43: 74LVC2G17, Package_TO_SOT_SMD:SOT-23-6, F.Cu at (266.5, 137.3)
- added U44: 74LVC2G17, Package_TO_SOT_SMD:SOT-23-6, F.Cu at (218.6, 89.4)
- added U45: 74LVC2G17, Package_TO_SOT_SMD:SOT-23-6, F.Cu at (225.1, 93.0)
- added U46: 74LVC2G17, Package_TO_SOT_SMD:SOT-23-6, F.Cu at (229.6, 95.7)
- added U47: 74LVC2G17, Package_TO_SOT_SMD:SOT-23-6, F.Cu at (234.3, 98.4)
- added U48: 74LVC2G17, Package_TO_SOT_SMD:SOT-23-6, F.Cu at (168.9, 80.8)
- added U49: 74LVC2G17, Package_TO_SOT_SMD:SOT-23-6, F.Cu at (176.4, 80.7)
- added U50: 74LVC2G17, Package_TO_SOT_SMD:SOT-23-6, F.Cu at (181.6, 80.7)
- added U51: 74LVC2G17, Package_TO_SOT_SMD:SOT-23-6, F.Cu at (187.0, 80.7)
- added U52: 74LVC2G17, Package_TO_SOT_SMD:SOT-23-6, F.Cu at (121.6, 98.3)
- added U53: 74LVC2G17, Package_TO_SOT_SMD:SOT-23-6, F.Cu at (128.0, 94.5)
- added U54: 74LVC2G17, Package_TO_SOT_SMD:SOT-23-6, F.Cu at (132.6, 91.8)
- added U55: 74LVC2G17, Package_TO_SOT_SMD:SOT-23-6, F.Cu at (137.3, 89.1)
- added U56: 74LVC2G17, Package_TO_SOT_SMD:SOT-23-6, F.Cu at (89.4, 137.0)
- added U57: 74LVC2G17, Package_TO_SOT_SMD:SOT-23-6, F.Cu at (93.0, 130.5)
- added U58: 74LVC2G17, Package_TO_SOT_SMD:SOT-23-6, F.Cu at (95.7, 126.0)
- added U59: 74LVC2G17, Package_TO_SOT_SMD:SOT-23-6, F.Cu at (98.4, 121.3)
- added U6: TXB0108PW, Package_SO:TSSOP-20_4.4x6.5mm_P0.65mm, F.Cu at (178.9, 284.6)
- added U60: 74LVC2G17, Package_TO_SOT_SMD:SOT-23-6, F.Cu at (80.8, 186.7)
- added U61: 74LVC2G17, Package_TO_SOT_SMD:SOT-23-6, F.Cu at (80.7, 179.2)
- added U62: 74LVC2G17, Package_TO_SOT_SMD:SOT-23-6, F.Cu at (80.7, 174.0)
- added U63: 74LVC2G17, Package_TO_SOT_SMD:SOT-23-6, F.Cu at (80.7, 168.6)
- added U64: 74LVC2G17, Package_TO_SOT_SMD:SOT-23-6, F.Cu at (98.3, 234.0)
- added U65: 74LVC2G17, Package_TO_SOT_SMD:SOT-23-6, F.Cu at (94.5, 227.6)
- added U66: 74LVC2G17, Package_TO_SOT_SMD:SOT-23-6, F.Cu at (91.8, 223.0)
- added U67: 74LVC2G17, Package_TO_SOT_SMD:SOT-23-6, F.Cu at (89.1, 218.3)
- added U68: 74LVC2G17, Package_TO_SOT_SMD:SOT-23-6, F.Cu at (137.0, 266.2)
- added U69: 74LVC2G17, Package_TO_SOT_SMD:SOT-23-6, F.Cu at (130.5, 262.6)
- added U7: TXB0108PW, Package_SO:TSSOP-20_4.4x6.5mm_P0.65mm, F.Cu at (285.2, 194.9)
- added U70: 74LVC2G17, Package_TO_SOT_SMD:SOT-23-6, F.Cu at (126.0, 259.9)
- added U71: 74LVC2G17, Package_TO_SOT_SMD:SOT-23-6, F.Cu at (121.3, 257.2)
- added U72: 74LVC2G17, Package_TO_SOT_SMD:SOT-23-6, F.Cu at (186.7, 274.8)
- added U73: 74LVC2G17, Package_TO_SOT_SMD:SOT-23-6, F.Cu at (179.2, 274.9)
- added U74: 74LVC2G17, Package_TO_SOT_SMD:SOT-23-6, F.Cu at (174.0, 274.9)
- added U75: 74LVC2G17, Package_TO_SOT_SMD:SOT-23-6, F.Cu at (168.6, 274.9)
- added U76: 74LVC2G17, Package_TO_SOT_SMD:SOT-23-6, F.Cu at (234.0, 257.3)
- added U77: 74LVC2G17, Package_TO_SOT_SMD:SOT-23-6, F.Cu at (227.6, 261.1)
- added U78: 74LVC2G17, Package_TO_SOT_SMD:SOT-23-6, F.Cu at (223.0, 263.8)
- added U79: 74LVC2G17, Package_TO_SOT_SMD:SOT-23-6, F.Cu at (218.3, 266.5)
- added U8: TXB0108PW, Package_SO:TSSOP-20_4.4x6.5mm_P0.65mm, F.Cu at (284.1, 224.3)
- added U80: 74LVC2G17, Package_TO_SOT_SMD:SOT-23-6, F.Cu at (266.2, 218.6)
- added U81: 74LVC2G17, Package_TO_SOT_SMD:SOT-23-6, F.Cu at (262.6, 225.1)
- added U82: 74LVC2G17, Package_TO_SOT_SMD:SOT-23-6, F.Cu at (259.9, 229.6)
- added U83: 74LVC2G17, Package_TO_SOT_SMD:SOT-23-6, F.Cu at (257.2, 234.3)
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- renumbered C16 to C100, C17 to C101, C18 to C102, C19 to C103, C20 to C104, C21 to C105, C22 to C106, C11 to C95, C12 to C96, C13 to C97, C14 to C98, C15 to C99
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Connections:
- net /Panel Headers/RESET renamed /Panel Headers/HDR_RESET
- C10 pad 1: +5V -> +3.3V
- C2 pad 1: +5V -> +3.3V
- C3 pad 1: +3.3V -> +5V
- C4 pad 1: +5V -> +3.3V
- C5 pad 1: +3.3V -> +5V
- C6 pad 1: +5V -> +3.3V
- C7 pad 1: +3.3V -> +5V
- C8 pad 1: +5V -> +3.3V
- C9 pad 1: +3.3V -> +5V
- P1 pad 10: /Level Shifters/PAN5V.CS_03 -> /Panel Headers/HDR_CS_03_P1
- P1 pad 11: /Level Shifters/PAN5V.CS_04 -> /Panel Headers/HDR_CS_04_P1
- P1 pad 15: /Level Shifters/PAN5V.EXT_INT -> /Panel Headers/HDR_EXT_INT_P1
- P1 pad 4: /Level Shifters/PAN5V.SCK_0 -> /Panel Headers/HDR_SCK_0_P1
- P1 pad 5: /Level Shifters/PAN5V.MOSI_0 -> /Panel Headers/HDR_MOSI_0_P1
- P1 pad 6: /Level Shifters/PAN5V.MISO_0 -> /Panel Headers/HDR_MISO_0_P1
- P1 pad 7: /Level Shifters/PAN5V.CS_00 -> /Panel Headers/HDR_CS_00_P1
- P1 pad 8: /Level Shifters/PAN5V.CS_01 -> /Panel Headers/HDR_CS_01_P1
- P1 pad 9: /Level Shifters/PAN5V.CS_02 -> /Panel Headers/HDR_CS_02_P1
- P10 pad 10: /Level Shifters/PAN5V.CS_18 -> /Panel Headers/HDR_CS_18_P10
- P10 pad 11: /Level Shifters/PAN5V.CS_19 -> /Panel Headers/HDR_CS_19_P10
- P10 pad 15: /Level Shifters/PAN5V.EXT_INT -> /Panel Headers/HDR_EXT_INT_P10
- P10 pad 4: /Level Shifters/PAN5V.SCK_1 -> /Panel Headers/HDR_SCK_1_P10
- P10 pad 5: /Level Shifters/PAN5V.MOSI_1 -> /Panel Headers/HDR_MOSI_1_P10
- P10 pad 6: /Level Shifters/PAN5V.MISO_1 -> /Panel Headers/HDR_MISO_1_P10
- P10 pad 7: /Level Shifters/PAN5V.CS_15 -> /Panel Headers/HDR_CS_15_P10
- P10 pad 8: /Level Shifters/PAN5V.CS_16 -> /Panel Headers/HDR_CS_16_P10
- P10 pad 9: /Level Shifters/PAN5V.CS_17 -> /Panel Headers/HDR_CS_17_P10
- P11 pad 10: /Level Shifters/PAN5V.CS_23 -> /Panel Headers/HDR_CS_23_P11
- P11 pad 11: /Level Shifters/PAN5V.CS_24 -> /Panel Headers/HDR_CS_24_P11
- P11 pad 15: /Level Shifters/PAN5V.EXT_INT -> /Panel Headers/HDR_EXT_INT_P11
- P11 pad 4: /Level Shifters/PAN5V.SCK_1 -> /Panel Headers/HDR_SCK_1_P11
- P11 pad 5: /Level Shifters/PAN5V.MOSI_1 -> /Panel Headers/HDR_MOSI_1_P11
- P11 pad 6: /Level Shifters/PAN5V.MISO_1 -> /Panel Headers/HDR_MISO_1_P11
- P11 pad 7: /Level Shifters/PAN5V.CS_20 -> /Panel Headers/HDR_CS_20_P11
- P11 pad 8: /Level Shifters/PAN5V.CS_21 -> /Panel Headers/HDR_CS_21_P11
- P11 pad 9: /Level Shifters/PAN5V.CS_22 -> /Panel Headers/HDR_CS_22_P11
- P12 pad 10: /Level Shifters/PAN5V.CS_28 -> /Panel Headers/HDR_CS_28_P12
- P12 pad 11: /Level Shifters/PAN5V.CS_29 -> /Panel Headers/HDR_CS_29_P12
- P12 pad 15: /Level Shifters/PAN5V.EXT_INT -> /Panel Headers/HDR_EXT_INT_P12
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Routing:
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- added copper zone on In2.Cu, net +3.3V
- added copper zone on In3.Cu, net +3.3V
- added copper zone on In4.Cu, net GND
- removed copper zone on In2.Cu, net +5V
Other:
- copper layers 4 -> 6
- board text added: "Teensy 12-12 Controller-Arena V0.1 R2"
- board text removed: "Teensy 12-12 Controller-Arena V0.1 R1"
